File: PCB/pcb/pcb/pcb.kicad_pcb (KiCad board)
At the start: 2 copper layers, 0 parts

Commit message: V0.75 all the footprints were set
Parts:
- added Arduino_Nano1: Arduino_Nano_v2.x, Module:Arduino_Nano, F.Cu at (152.2, 95.4)
- added Arduino_power_plug1: Conn_01x03_Female, Connector_BarrelJack:BarrelJack_Horizontal, F.Cu at (186.5, 94.9)
- added D1: LED, LED_THT:LED_D3.0mm_FlatTop, F.Cu at (194.4, 129.9)
- added D2: LED, LED_THT:LED_D3.0mm_FlatTop, F.Cu at (194.4, 123.1)
- added D3: LED, LED_THT:LED_D3.0mm_FlatTop, F.Cu at (194.4, 116.2)
- added D4: LED, LED_THT:LED_D3.0mm_FlatTop, F.Cu at (194.4, 109.4)
- added LED'sDriver1: ULN2003A, Package_DIP:DIP-16_W7.62mm_LongPads, F.Cu at (177.6, 110.9)
- added MK1: M2.5, MountingHole:MountingHole_2.7mm_M2.5, F.Cu at (121.3, 86.5)
- added MK2: M2.5, MountingHole:MountingHole_2.7mm_M2.5, F.Cu at (121.3, 121.3)
- added MK3: M2.5, MountingHole:MountingHole_2.7mm_M2.5, F.Cu at (197.2, 96.4)
- added MK4: M2.5, MountingHole:MountingHole_2.7mm_M2.5, F.Cu at (201.8, 143.4)
- added MK5: M2.5, MountingHole:MountingHole_2.7mm_M2.5, F.Cu at (124.1, 154.6)
- added MK6: M2.5, MountingHole:MountingHole_2.7mm_M2.5, F.Cu at (197.5, 85.2)
- added MK7: M2.5, MountingHole:MountingHole_2.7mm_M2.5, F.Cu at (163.9, 85.2)
- added MK8: M2.5, MountingHole:MountingHole_2.7mm_M2.5, F.Cu at (172.6, 134.0)
- added Motor1: TMC2100, Motor_driver:IC_DRV8825_STEPPER_MOTOR_DRIVER_CARRIER, F.Cu at (137.0, 102.0)
- added Motor2: TMC2100, Motor_driver:IC_DRV8825_STEPPER_MOTOR_DRIVER_CARRIER, F.Cu at (137.5, 126.4)
- added Motor_power_plug1: Conn_01x03_Female, Connector_BarrelJack:BarrelJack_Horizontal, F.Cu at (138.0, 142.1)
- added R1: 10K, Resistor_THT:R_Axial_DIN0207_L6.3mm_D2.5mm_P7.62mm_Horizontal, F.Cu at (162.5, 138.6)
- added R2: 10K, Resistor_THT:R_Axial_DIN0207_L6.3mm_D2.5mm_P7.62mm_Horizontal, F.Cu at (157.0, 138.6)
- added R3: 10K, Resistor_THT:R_Axial_DIN0207_L6.3mm_D2.5mm_P7.62mm_Horizontal, F.Cu at (151.5, 138.6)
- added R4: 10K, Resistor_THT:R_Axial_DIN0207_L6.3mm_D2.5mm_P7.62mm_Horizontal, F.Cu at (168.0, 138.6)
- added R5: 220, Resistor_THT:R_Axial_DIN0207_L6.3mm_D2.5mm_P7.62mm_Horizontal, F.Cu at (207.4, 129.9)
- added R6: 220, Resistor_THT:R_Axial_DIN0207_L6.3mm_D2.5mm_P7.62mm_Horizontal, F.Cu at (207.4, 122.8)
- added R7: 220, Resistor_THT:R_Axial_DIN0207_L6.3mm_D2.5mm_P7.62mm_Horizontal, F.Cu at (207.4, 116.2)
- added R8: 220, Resistor_THT:R_Axial_DIN0207_L6.3mm_D2.5mm_P7.62mm_Horizontal, F.Cu at (207.4, 109.4)
- added limit_swtich1: Conn_01x03_Female, Connector_PinHeader_2.54mm:PinHeader_1x03_P2.54mm_Vertical, F.Cu at (174.6, 154.3)
- added limit_swtich2: Conn_01x03_Female, Connector_PinHeader_2.54mm:PinHeader_1x03_P2.54mm_Vertical, F.Cu at (164.7, 154.6)
- added limit_swtich3: Conn_01x03_Female, Connector_PinHeader_2.54mm:PinHeader_1x03_P2.54mm_Vertical, F.Cu at (154.3, 154.6)
- added limit_swtich4: Conn_01x03_Female, Connector_PinHeader_2.54mm:PinHeader_1x03_P2.54mm_Vertical, F.Cu at (184.5, 154.6)
- added motor1_plug1: Conn_01x04_Male, Connector_PinHeader_2.54mm:PinHeader_1x04_P2.54mm_Vertical, F.Cu at (126.8, 105.8)
- added motor2_plug1: Conn_01x04_Male, Connector_PinHeader_2.54mm:PinHeader_1x04_P2.54mm_Vertical, F.Cu at (127.6, 130.2)
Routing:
- net +5V: track 0.00 -> 246.3 mm, vias 0 -> 1
- net GND: track 0.00 -> 219.6 mm, vias 0 -> 2
- net GND_motor: track 0.00 -> 66.2 mm
- net Limit_switch1: track 0.00 -> 47.0 mm
- net Limit_switch2: track 0.00 -> 41.7 mm
- net Vmot_1: track 0.00 -> 37.6 mm
- net Limit_switch4: track 0.00 -> 32.4 mm
- net Limit_switch3: track 0.00 -> 26.6 mm
- net Step_motor1: track 0.00 -> 22.1 mm
- net Dir_motor1: track 0.00 -> 21.2 mm
- net EN_motor2: track 0.00 -> 17.3 mm
- net S_LED1: track 0.00 -> 16.0 mm
- net S_LED2: track 0.00 -> 12.7 mm
- net S_LED3: track 0.00 -> 10.9 mm
- net EN_motor1: track 0.00 -> 10.9 mm
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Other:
- board outline added: 94.5 x 79.2 mm

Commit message: V0.8 this commit close #5 also fixes #6
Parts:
- removed MK5, MK6, MK7, MK8: M2.5, MountingHole:MountingHole_2.7mm_M2.5
- moved MK2 89.2 mm to (198.0, 166.8), turned to 0 degrees
- moved MK3 79.0 mm to (239.4, 163.2)
- moved MK1 78.3 mm to (182.5, 135.3), turned to 0 degrees
- moved LED'sDriver1 68.9 mm to (243.4, 131.5), turned to 270 degrees
- moved R1 63.5 mm to (222.4, 159.7), turned to 180 degrees
- moved R4 59.8 mm to (222.1, 164.0), turned to 180 degrees
- moved Motor1 59.7 mm to (192.6, 123.6)
- moved motor1_plug1 59.4 mm to (182.2, 127.4)
- moved D4 59.3 mm to (243.2, 143.1), turned to 270 degrees
- moved R8 59.1 mm to (243.2, 156.3), turned to 90 degrees
- moved Motor2 58.7 mm to (192.6, 146.7)
- moved motor2_plug1 58.4 mm to (182.2, 150.8)
- moved Motor_power_plug1 58.3 mm to (191.9, 164.5), turned to 0 degrees
- moved Arduino_Nano1 58.1 mm to (206.1, 117.2)
- moved limit_swtich4 57.4 mm to (239.9, 169.8)
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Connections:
- Arduino_Nano1 pad 13: Limit_switch1 -> Limit_switch4
- Arduino_Nano1 pad 14: Limit_switch2 -> Limit_switch3
- Arduino_Nano1 pad 15: Limit_switch3 -> Limit_switch2
- Arduino_Nano1 pad 16: Limit_switch4 -> Limit_switch1
- LED'sDriver1 pad 1: LED4 -> LED1
- LED'sDriver1 pad 2: LED3 -> LED2
- LED'sDriver1 pad 3: LED2 -> LED3
- LED'sDriver1 pad 4: LED1 -> LED4
- Motor2 pad 16: Vmot_2 -> Vmot_1
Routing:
- net GND: track 219.6 -> 26.8 mm, vias 2 -> 0
- net +5V: track 246.3 -> 220.5 mm, vias 1 -> 0
- net LED1: track 10.3 -> 26.5 mm
- net LED2: track 10.3 -> 22.9 mm
- net Limit_switch2: track 41.7 -> 30.4 mm
- net Limit_switch1: track 47.0 -> 38.0 mm
- net LED3: track 10.3 -> 19.3 mm
- net Vmot_1: track 37.6 -> 45.5 mm
- net Limit_switch3: track 26.6 -> 19.8 mm
- net LED4: track 10.3 -> 16.6 mm
- net S_LED4: track 10.4 -> 4.17 mm
- net S_LED3: track 10.9 -> 5.81 mm
- net GND_motor: track 66.2 -> 71.1 mm
- net S_LED2: track 12.7 -> 8.33 mm
- net S_LED1: track 16.0 -> 11.9 mm
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- added copper zone on B.Cu, net GND
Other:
- board size 94.5 x 79.2 mm -> 69.6 x 60.2 mm

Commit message: V0.8 pcb Finished this closes #9 and closes #8
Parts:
- removed MK2: M2.5, MountingHole:MountingHole_2.7mm_M2.5
- moved MK1 65.1 mm to (244.2, 114.7)
- moved MK4 48.1 mm to (180.9, 135.3)
- moved MK3 42.1 mm to (197.7, 169.3)
- moved limit_swtich3 35.2 mm to (242.9, 162.7)
- moved limit_swtich2 24.2 mm to (242.9, 168.0)
- moved limit_swtich4 10.6 mm to (232.0, 162.7)
- moved R2 8.76 mm to (211.2, 161.4), turned to 270 degrees
- moved R1 6.35 mm to (216.3, 161.4), turned to 270 degrees
- moved Arduino_power_plug1 3.84 mm to (234.0, 123.8)
- moved R3 3.75 mm to (206.1, 161.4), turned to 270 degrees
- moved limit_swtich1 3.31 mm to (232.0, 168.0)
- moved R4 2.65 mm to (221.3, 161.4), turned to 270 degrees
- moved motor2_plug1 0.25 mm to (182.2, 150.5)
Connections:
- Arduino_Nano1 pad 13: Limit_switch4 -> Net-(Arduino_Nano1-Pad13)
- Arduino_Nano1 pad 14: Limit_switch3 -> Limit_switch2
- Arduino_Nano1 pad 15: Limit_switch2 -> Limit_switch3
- Arduino_Nano1 pad 16: Limit_switch1 -> Limit_switch4
- Arduino_Nano1 pad 19: Net-(Arduino_Nano1-Pad19) -> Limit_switch1
- Arduino_Nano1 pad 4: GND -> Net-(Arduino_Nano1-Pad4)
- Arduino_power_plug1 pad 2: Net-(Arduino_power_plug1-Pad2) -> GND
- Motor_power_plug1 pad 2: Net-(Motor_power_plug1-Pad2) -> GND_motor
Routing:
- net +5V: track 220.5 -> 188.4 mm
- net GND: track 26.8 -> 0.00 mm
- net Limit_switch1: track 38.0 -> 18.4 mm
- net Limit_switch2: track 30.4 -> 13.2 mm
- net Limit_switch4: track 30.3 -> 14.8 mm
- net Limit_switch3: track 19.8 -> 8.74 mm
- net Vmot_1: track 45.5 -> 40.6 mm
- net GND_motor: track 71.1 -> 67.7 mm
- net Step_motor1: track 20.7 -> 21.8 mm
- net Dir_motor1: track 21.3 -> 22.2 mm
- net S_LED1: track 11.9 -> 12.8 mm
- net S_LED2: track 8.33 -> 8.97 mm
- removed copper zone on B.Cu, net GND
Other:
- board size 69.6 x 60.2 mm -> 70.9 x 62.7 mm
- net class Default: clearance 0.2 -> 0.25; trace_width 0.2 -> 0.4
- net class Power: clearance 0.2 -> 0.25; trace_width 0.5 -> 0.4
- rule trace_clearance: 0.2 -> 0.25
- rule trace_min: 0.1524 -> 0.2

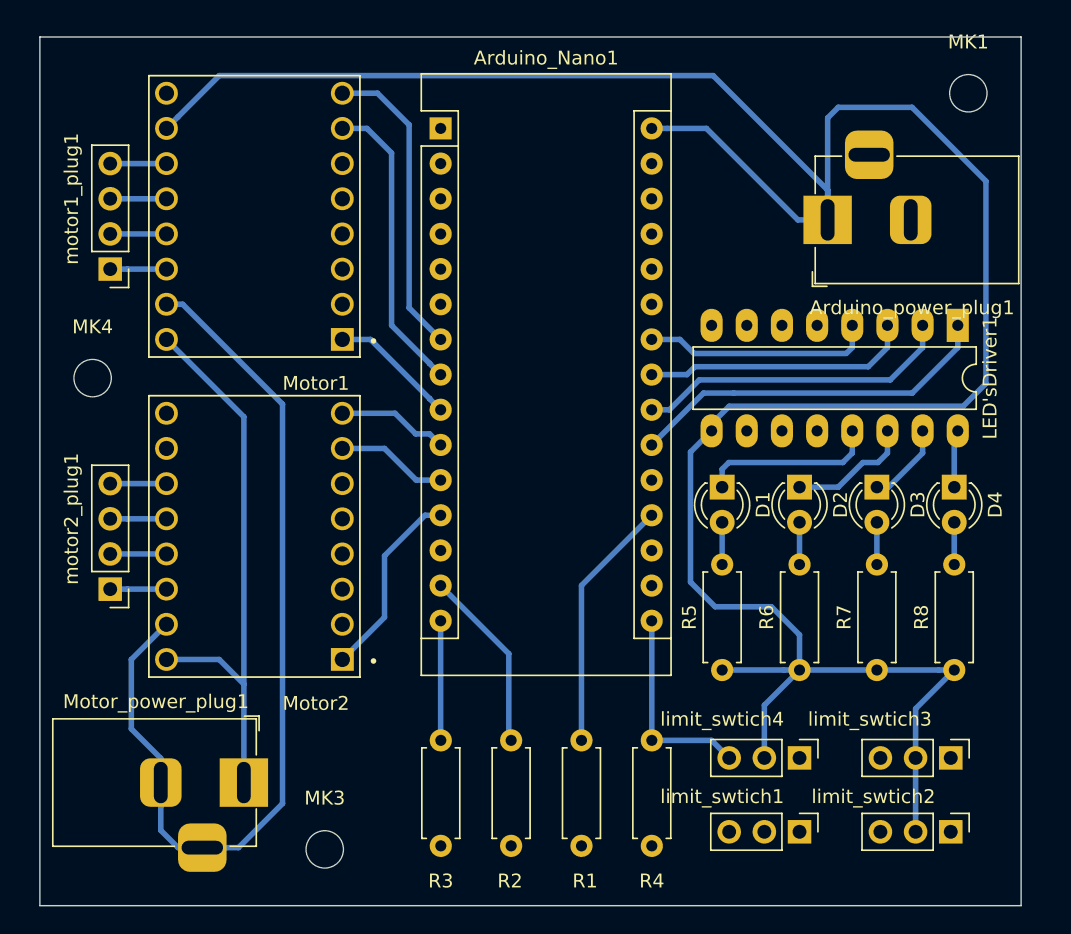
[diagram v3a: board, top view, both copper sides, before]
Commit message: V0.82 the gerbers were generated and sent to fabrication that close #7
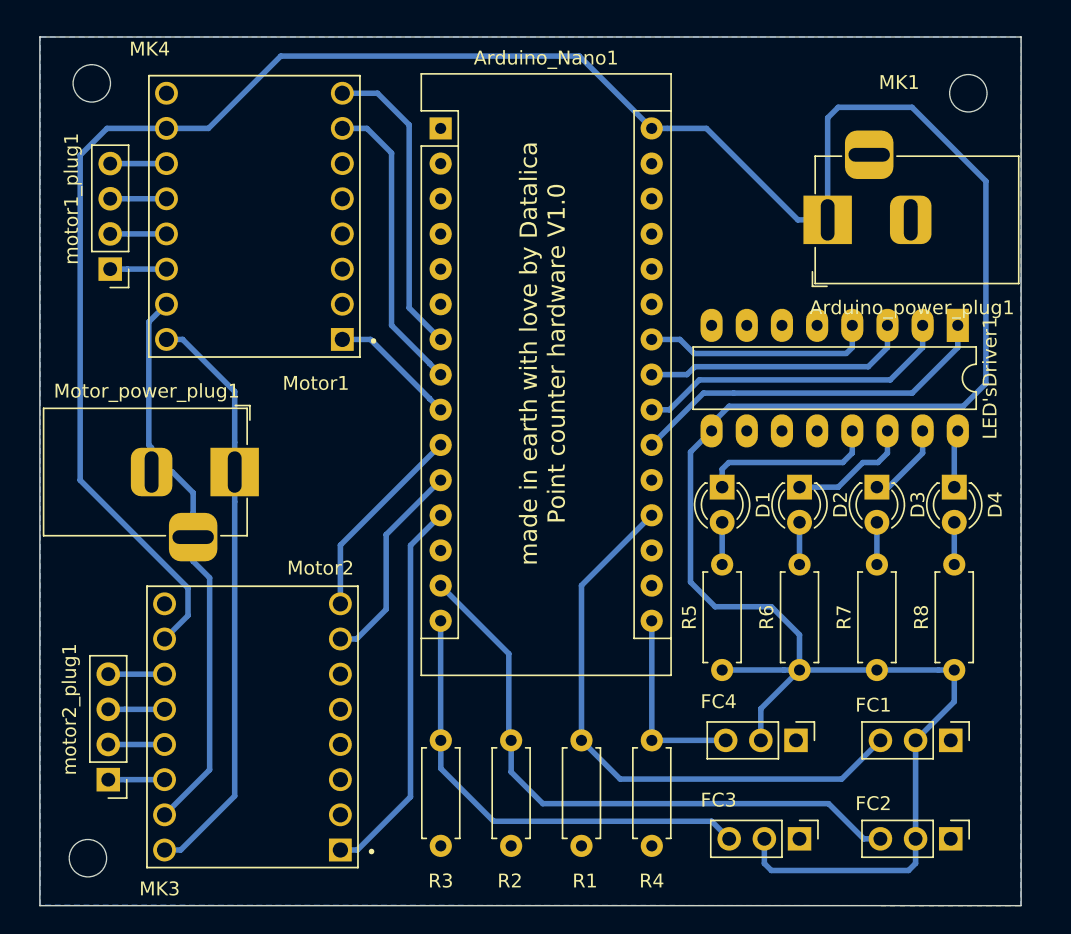
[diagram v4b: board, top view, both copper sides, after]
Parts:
- moved Motor_power_plug1 22.4 mm to (191.2, 142.1)
- moved MK4 21.3 mm to (180.9, 114.0)
- moved MK3 17.1 mm to (180.6, 169.9)
- moved Motor2 13.8 mm to (192.5, 160.5)
- moved motor2_plug1 13.8 mm to (182.1, 164.3)
- moved FC1 12.8 mm to (242.9, 161.4)
- moved FC3 12.4 mm to (232.0, 168.5)
- moved FC4 1.30 mm to (231.8, 161.4)
- moved FC2 0.51 mm to (242.9, 168.5)
- renumbered limit_swtich1 to FC1, limit_swtich2 to FC2, limit_swtich3 to FC3, limit_swtich4 to FC4
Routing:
- net +5V: track 188.4 -> 233.0 mm
- net Limit_switch2: track 13.2 -> 44.2 mm
- net GND_motor: track 67.7 -> 41.4 mm
- net Limit_switch3: track 8.74 -> 33.7 mm
- net Limit_switch1: track 18.4 -> 42.3 mm
- net EN_motor2: track 14.0 -> 27.9 mm
- net Step_motor2: track 8.05 -> 15.2 mm
- net Dir_motor2: track 8.05 -> 14.5 mm
- net Vmot_1: track 40.6 -> 42.4 mm
- net Limit_switch4: track 14.8 -> 14.0 mm
- added copper zone on B.Cu, net GND
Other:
- board text added: "made in earth with love by Datalica Point counter hardware V1.0"
